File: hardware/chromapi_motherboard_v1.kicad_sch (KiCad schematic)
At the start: 8 parts

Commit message: Annotating components
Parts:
- renumbered FID3 to FID2, FID2 to FID3, TP10 to TP1
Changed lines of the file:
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@@
 		(dnp no)
 		(fields_autoplaced yes)
-		(property "Reference" "#FLG04"
+		(property "Reference" "#FLG01"
 			(at 162.56 186.055 0)
 			(effects
@@
 			(project "chromapi_motherboard_v1"
 				(path "/d1a31f26-03e0-43e1-89c1-031fe31befc5"
-					(reference "#FLG04")
+					(reference "#FLG01")
 					(unit 1)
 				)
@@
 		(dnp no)
 		(fields_autoplaced yes)
-		(property "Reference" "FID2"
+		(property "Reference" "FID3"
 			(at 128.27 175.2599 0)
 			(effects
@@
 			(project "chromapi_motherboard_v1"
 				(path "/d1a31f26-03e0-43e1-89c1-031fe31befc5"
-					(reference "FID2")
+					(reference "FID3")
 					(unit 1)
 				)
@@
 		(dnp no)
 		(fields_autoplaced yes)
-		(property "Reference" "FID3"
+		(property "Reference" "FID2"
 			(at 123.19 182.8799 0)
 			(effects
@@
 			(project "chromapi_motherboard_v1"
 				(path "/d1a31f26-03e0-43e1-89c1-031fe31befc5"
-					(reference "FID3")
+					(reference "FID2")
 					(unit 1)
 				)
@@
 		(dnp no)
 		(fields_autoplaced yes)
-		(property "Reference" "TP10"
+		(property "Reference" "TP1"
 			(at 137.668 177.8 90)
 			(effects
@@
 			(project ""
 				(path "/d1a31f26-03e0-43e1-89c1-031fe31befc5"
-					(reference "TP10")
-					(unit 1)
-				)
+					(reference "TP1")
+					(unit 1)
+				)

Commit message: Adding footprint & symbol folders
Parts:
- renumbered FID3 to FID2, FID2 to FID3
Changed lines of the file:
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@@
 		(dnp no)
 		(fields_autoplaced yes)
-		(property "Reference" "FID3"
+		(property "Reference" "FID2"
 			(at 128.27 175.2599 0)
 			(effects
@@
 			(project "chromapi_motherboard_v1"
 				(path "/d1a31f26-03e0-43e1-89c1-031fe31befc5"
-					(reference "FID3")
+					(reference "FID2")
 					(unit 1)
 				)
@@
 		(dnp no)
 		(fields_autoplaced yes)
-		(property "Reference" "FID2"
+		(property "Reference" "FID3"
 			(at 123.19 182.8799 0)
 			(effects
@@
 			(project "chromapi_motherboard_v1"
 				(path "/d1a31f26-03e0-43e1-89c1-031fe31befc5"
-					(reference "FID2")
+					(reference "FID3")
 					(unit 1)
 				)

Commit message: Updating footprints
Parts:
- FID1, FID2, FID3: footprint (none) -> Fiducial:Fiducial_1mm_Mask2mm
- H1, H2, H3, H4: footprint (none) -> MountingHole:MountingHole_2.7mm_M2.5_ISO14580_Pad_TopBottom
- TP1: footprint (none) -> TestPoint:TestPoint_Pad_D1.5mm
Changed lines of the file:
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@@
 			)
 		)
-		(property "Footprint" ""
+		(property "Footprint" "MountingHole:MountingHole_2.7mm_M2.5_ISO14580_Pad_TopBottom"
 			(at 156.21 177.8 0)
 			(effects
@@
 			)
 		)
-		(property "Footprint" ""
+		(property "Footprint" "Fiducial:Fiducial_1mm_Mask2mm"
 			(at 125.73 176.53 0)
 			(effects
@@
 			)
 		)
-		(property "Footprint" ""
+		(property "Footprint" "MountingHole:MountingHole_2.7mm_M2.5_ISO14580_Pad_TopBottom"
 			(at 149.86 177.8 0)
 			(effects
@@
 			)
 		)
-		(property "Footprint" ""
+		(property "Footprint" "Fiducial:Fiducial_1mm_Mask2mm"
 			(at 120.65 184.15 0)
 			(effects
@@
 			)
 		)
-		(property "Footprint" ""
+		(property "Footprint" "Fiducial:Fiducial_1mm_Mask2mm"
 			(at 115.57 176.53 0)
 			(effects
@@
 			)
 		)
-		(property "Footprint" ""
+		(property "Footprint" "MountingHole:MountingHole_2.7mm_M2.5_ISO14580_Pad_TopBottom"
 			(at 143.51 177.8 0)
 			(effects
@@
 			)
 		)
-		(property "Footprint" ""
+		(property "Footprint" "TestPoint:TestPoint_Pad_D1.5mm"
 			(at 140.97 177.8 0)
 			(effects
@@
 			)
 		)
-		(property "Footprint" ""
+		(property "Footprint" "MountingHole:MountingHole_2.7mm_M2.5_ISO14580_Pad_TopBottom"
 			(at 162.56 177.8 0)
 			(effects

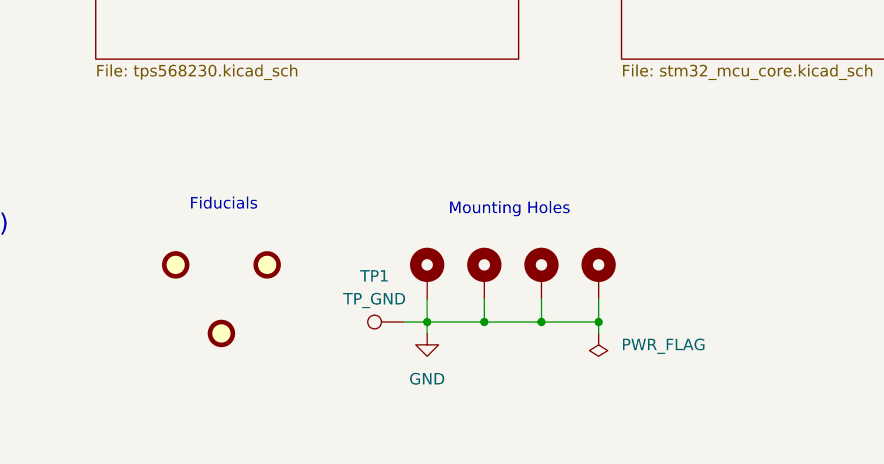
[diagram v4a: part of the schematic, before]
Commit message: adding chromapi logo to library
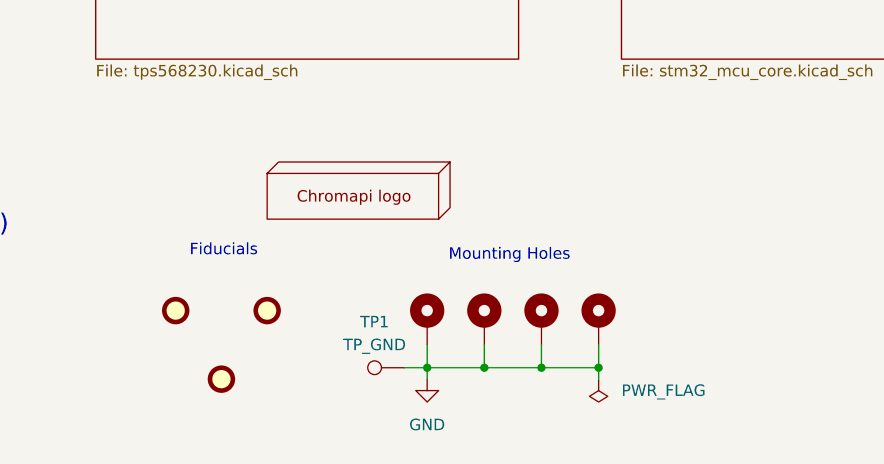
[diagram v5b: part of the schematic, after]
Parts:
- added H1: ~, Chromapi_FP:chromapi_logo, symbol chromapi_logo:Chromapi_Logo
- renumbered H1 to H2, H2 to H3, H3 to H4, H4 to H5
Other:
- moved on the sheet: TP1

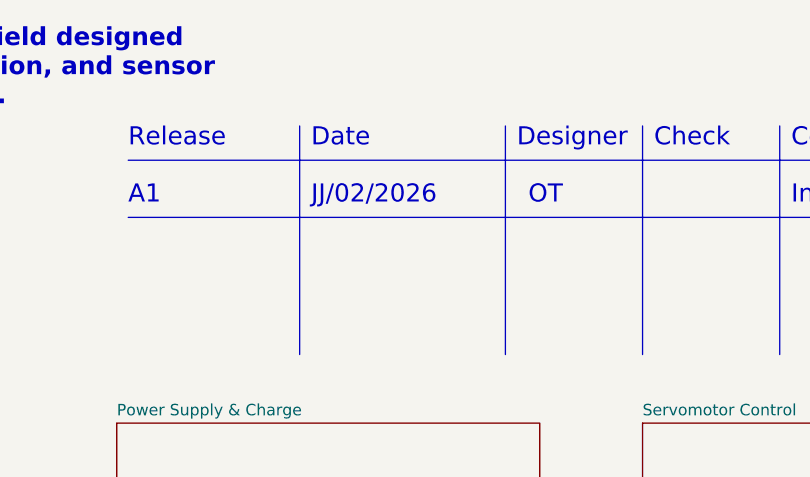
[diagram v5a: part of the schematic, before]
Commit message: Applying first corrections from first review
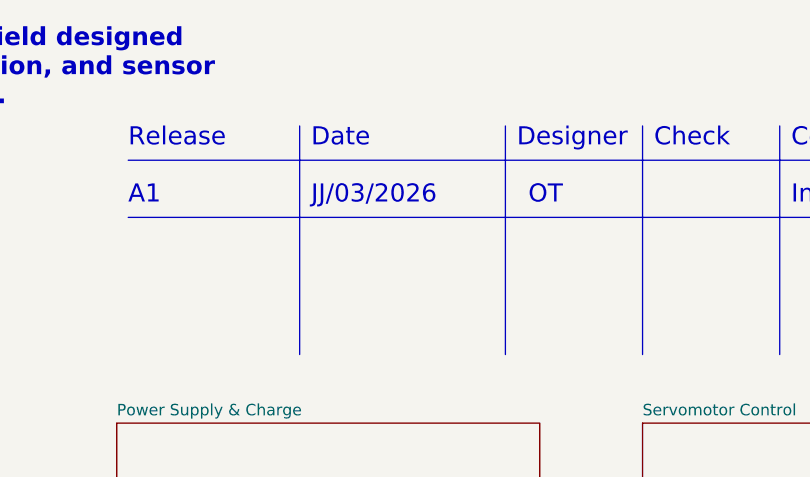
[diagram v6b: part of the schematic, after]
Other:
- note added: "JJ/03/2026"
- note removed: "JJ/02/2026"
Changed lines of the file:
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@@
 		)
 	)
-	(text "JJ/02/2026"
+	(text "JJ/03/2026"
 		(exclude_from_sim no)
 		(at 128.27 35.56 0)

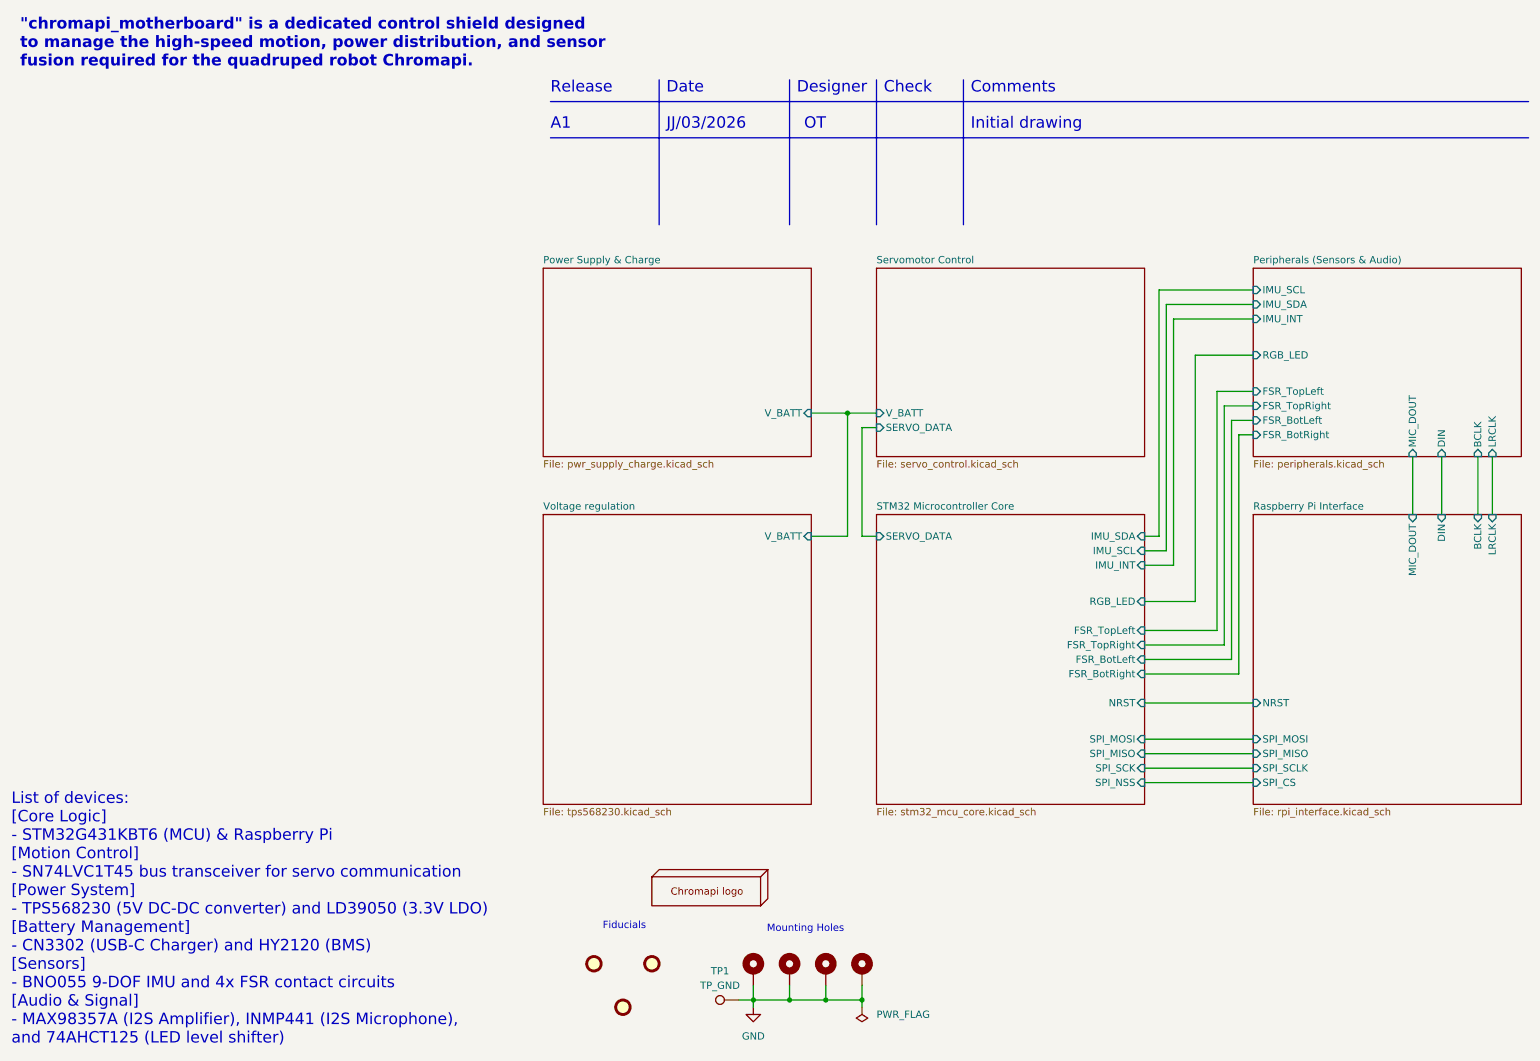
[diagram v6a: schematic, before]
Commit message: Schematic servo tranceiver correction
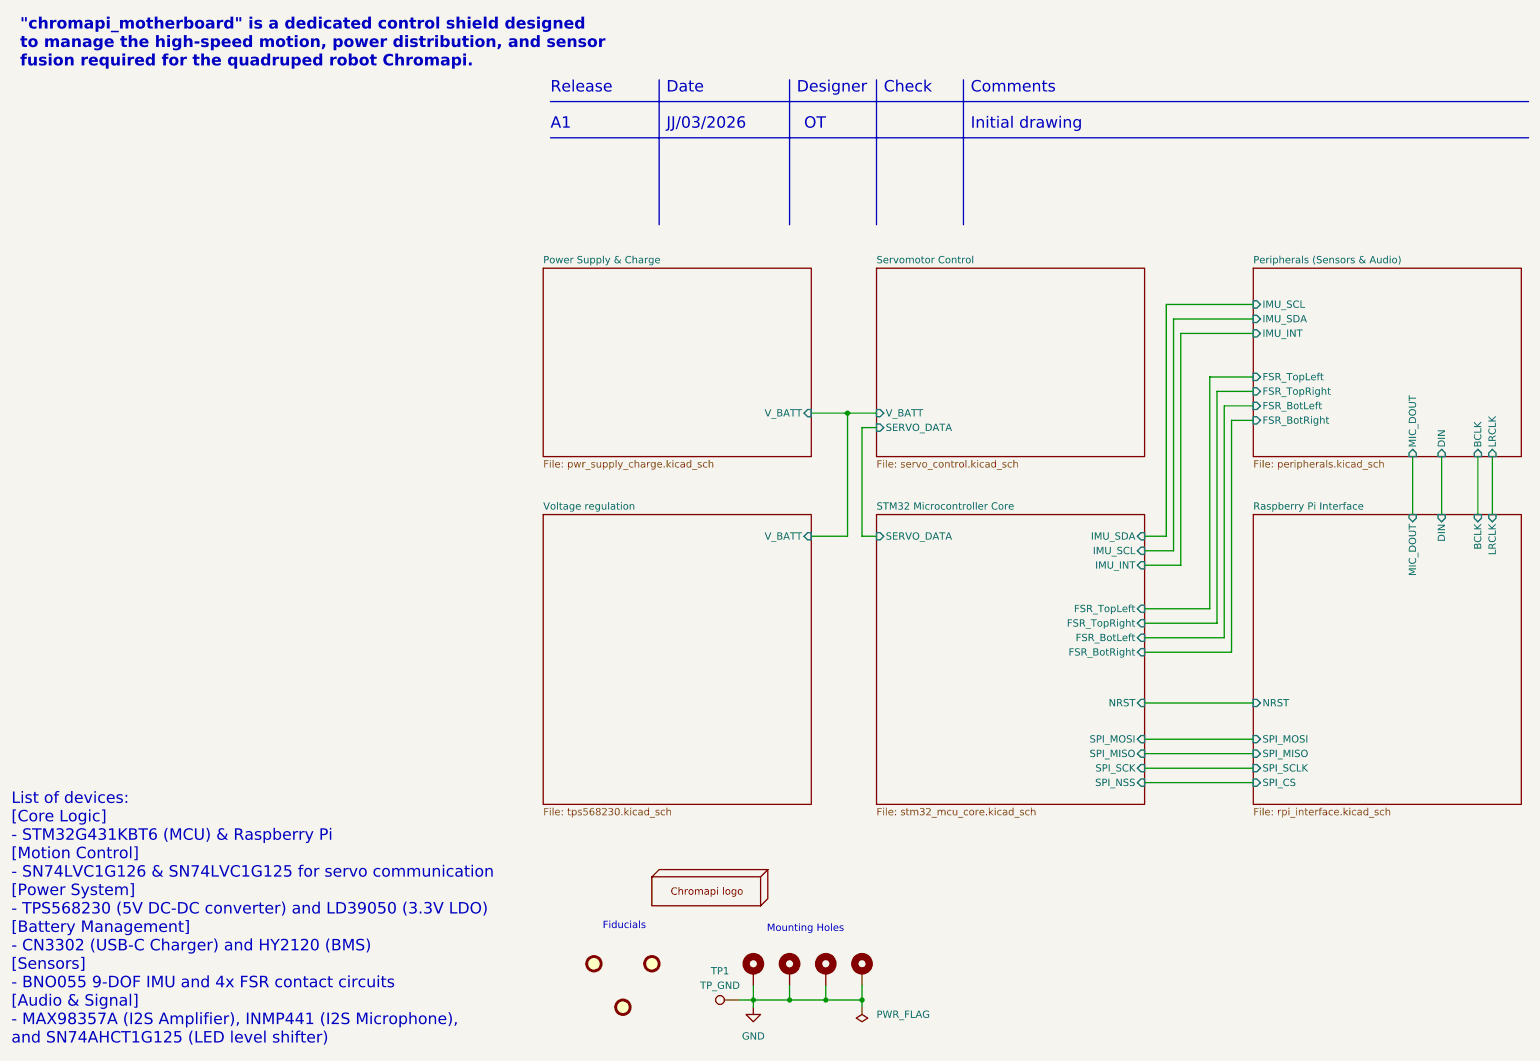
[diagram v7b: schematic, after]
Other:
- sheet Peripherals (Sensors & Audio) ports: added none; removed RGB_LED
- sheet STM32 Microcontroller Core ports: added none; removed RGB_LED
- note added: "List of devices: [Core Logic] - STM32G431KBT6 (MCU) & Raspberry Pi [Motion Control] - SN74LVC1G126 & SN74LVC1G125 for servo communication [Power System] - TPS568230 (5V DC-DC converter) and LD39050 (3.3V LDO) [Battery Management] - CN3302 (USB-C Charger) and HY2120 (BMS) [Sensors] - BNO055 9-DOF IMU and 4x FSR contact circuits [Audio & Signal] - MAX98357A (I2S Amplifier), INMP441 (I2S Microphone)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"
- note removed: "List of devices: [Core Logic] - STM32G431KBT6 (MCU) & Raspberry Pi [Motion Control] - SN74LVC1T45 bus transceiver for servo communication [Power System] - TPS568230 (5V DC-DC converter) and LD39050 (3.3V LDO) [Battery Management] - CN3302 (USB-C Charger) and HY2120 (BMS) [Sensors] - BNO055 9-DOF IMU and 4x FSR contact circuits [Audio & Signal] - MAX98357A (I2S Amplifier), INMP441 (I2S Microphone)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"
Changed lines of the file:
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@@
 		)
 	)
-	(text "List of devices:\n[Core Logic] \n- STM32G431KBT6 (MCU) & Raspberry Pi\n[Motion Control] \n- SN74LVC1T45 bus transceiver for servo communication\n[Power System] \n- TPS568230 (5V DC-DC converter) and LD39050 (3.3V LDO)\n[Battery Management] \n- CN3302 (USB-C Charger) and HY2120 (BMS)\n[Sensors] \n- BNO055 9-DOF IMU and 4x FSR contact circuits\n[Audio & Signal] \n- MAX98357A (I2S Amplifier), INMP441 (I2S Microphone),\nand 74AHCT125 (LED level shifter)"
+	(text "List of devices:\n[Core Logic] \n- STM32G431KBT6 (MCU) & Raspberry Pi\n[Motion Control] \n- SN74LVC1G126 & SN74LVC1G125 for servo communication\n[Power System] \n- TPS568230 (5V DC-DC converter) and LD39050 (3.3V LDO)\n[Battery Management] \n- CN3302 (USB-C Charger) and HY2120 (BMS)\n[Sensors] \n- BNO055 9-DOF IMU and 4x FSR contact circuits\n[Audio & Signal] \n- MAX98357A (I2S Amplifier), INMP441 (I2S Microphone),\nand SN74AHCT1G125 (LED level shifter)"
 		(exclude_from_sim no)
 		(at 13.462 173.736 0)
@@
 	(wire
 		(pts
-			(xy 212.09 106.68) (xy 214.63 106.68)
+			(xy 212.09 106.68) (xy 215.9 106.68)
 		)
 		(stroke
@@
 	(wire
 		(pts
-			(xy 227.33 86.36) (xy 227.33 128.27)
+			(xy 226.06 83.82) (xy 226.06 124.46)
 		)
 		(stroke
@@
 	(wire
 		(pts
-			(xy 215.9 109.22) (xy 215.9 66.04)
+			(xy 217.17 109.22) (xy 217.17 68.58)
 		)
 		(stroke
@@
 	(wire
 		(pts
-			(xy 217.17 111.76) (xy 212.09 111.76)
+			(xy 218.44 111.76) (xy 212.09 111.76)
 		)
 		(stroke
@@
 	(wire
 		(pts
-			(xy 231.14 83.82) (xy 226.06 83.82)
+			(xy 231.14 81.28) (xy 224.79 81.28)
 		)
 		(stroke
@@
 	(wire
 		(pts
-			(xy 227.33 128.27) (xy 212.09 128.27)
+			(xy 226.06 124.46) (xy 212.09 124.46)
 		)
 		(stroke
@@
 	(wire
 		(pts
-			(xy 212.09 118.11) (xy 220.98 118.11)
-		)
-		(stroke
-			(width 0)
-			(type default)
-		)
-	)
-	(wire
-		(pts
-			(xy 231.14 68.58) (xy 217.17 68.58)
+			(xy 231.14 71.12) (xy 218.44 71.12)
 		)
 		(stroke
@@
 	(wire
 		(pts
-			(xy 214.63 106.68) (xy 214.63 63.5)
+			(xy 215.9 106.68) (xy 215.9 66.04)
 		)
 		(stroke
@@
 	(wire
 		(pts
-			(xy 217.17 68.58) (xy 217.17 111.76)
+			(xy 218.44 71.12) (xy 218.44 111.76)
 		)
 		(stroke
@@
 	(wire
 		(pts
-			(xy 231.14 86.36) (xy 227.33 86.36)
+			(xy 231.14 83.82) (xy 226.06 83.82)
 		)
 		(stroke
@@
 	(wire
 		(pts
-			(xy 220.98 74.93) (xy 231.14 74.93)
-		)
-		(stroke
-			(width 0)
-			(type default)
-		)
-	)
-	(wire
-		(pts
 			(xy 259.08 92.71) (xy 259.08 102.87)
 		)
@@
 	(wire
 		(pts
-			(xy 228.6 130.81) (xy 228.6 88.9)
+			(xy 227.33 127) (xy 227.33 86.36)
 		)
 		(stroke
@@
 	(wire
 		(pts
-			(xy 226.06 83.82) (xy 226.06 125.73)
+			(xy 224.79 81.28) (xy 224.79 121.92)
 		)
 		(stroke
@@
 	(wire
 		(pts
-			(xy 224.79 81.28) (xy 231.14 81.28)
+			(xy 223.52 78.74) (xy 231.14 78.74)
 		)
 		(stroke
@@
 	(wire
 		(pts
-			(xy 220.98 118.11) (xy 220.98 74.93)
-		)
-		(stroke
-			(width 0)
-			(type default)
-		)
-	)
-	(wire
-		(pts
 			(xy 212.09 144.78) (xy 231.14 144.78)
 		)
@@
 	(wire
 		(pts
-			(xy 228.6 88.9) (xy 231.14 88.9)
+			(xy 227.33 86.36) (xy 231.14 86.36)
 		)
 		(stroke
@@
 	(wire
 		(pts
-			(xy 214.63 63.5) (xy 231.14 63.5)
+			(xy 215.9 66.04) (xy 231.14 66.04)
 		)
 		(stroke
@@
 	(wire
 		(pts
-			(xy 224.79 123.19) (xy 224.79 81.28)
+			(xy 223.52 119.38) (xy 223.52 78.74)
 		)
 		(stroke
@@
 	(wire
 		(pts
-			(xy 212.09 123.19) (xy 224.79 123.19)
+			(xy 212.09 119.38) (xy 223.52 119.38)
 		)
 		(stroke
@@
 	(wire
 		(pts
-			(xy 212.09 109.22) (xy 215.9 109.22)
+			(xy 212.09 109.22) (xy 217.17 109.22)
 		)
 		(stroke
@@
 	(wire
 		(pts
-			(xy 215.9 66.04) (xy 231.14 66.04)
+			(xy 217.17 68.58) (xy 231.14 68.58)
 		)
 		(stroke
@@
 	(wire
 		(pts
-			(xy 212.09 130.81) (xy 228.6 130.81)
+			(xy 212.09 127) (xy 227.33 127)
 		)
 		(stroke
@@
 	(wire
 		(pts
-			(xy 226.06 125.73) (xy 212.09 125.73)
+			(xy 224.79 121.92) (xy 212.09 121.92)
 		)
 		(stroke
@@
 		)
 		(pin "FSR_TopRight" input
-			(at 212.09 125.73 0)
+			(at 212.09 121.92 0)
 			(effects
 				(font
@@
 		)
 		(pin "FSR_TopLeft" input
-			(at 212.09 123.19 0)
+			(at 212.09 119.38 0)
 			(effects
 				(font
@@
 		)
 		(pin "FSR_BotLeft" input
-			(at 212.09 128.27 0)
-			(effects
-				(font
-					(size 1.27 1.27)
-				)
-				(justify right)
-			)
-		)
-		(pin "RGB_LED" input
-			(at 212.09 118.11 0)
+			(at 212.09 124.46 0)
 			(effects
 				(font
@@
 		)
 		(pin "FSR_BotRight" input
-			(at 212.09 130.81 0)
+			(at 212.09 127 0)
 			(effects
 				(font
@@
 			)
 		)
-		(pin "RGB_LED" input
-			(at 231.14 74.93 180)
-			(effects
-				(font
-					(size 1.27 1.27)
-				)
-				(justify left)
-			)
-		)
 		(pin "FSR_TopLeft" input
-			(at 231.14 81.28 180)
+			(at 231.14 78.74 180)
 			(effects
 				(font
@@
 		)
 		(pin "FSR_TopRight" input
-			(at 231.14 83.82 180)
+			(at 231.14 81.28 180)
 			(effects
 				(font
@@
 		)
 		(pin "IMU_SCL" input
-			(at 231.14 63.5 180)
+			(at 231.14 66.04 180)
 			(effects
 				(font
@@
 		)
 		(pin "IMU_INT" input
-			(at 231.14 68.58 180)
+			(at 231.14 71.12 180)
 			(effects
 				(font
@@
 		)
 		(pin "FSR_BotLeft" input
-			(at 231.14 86.36 180)
+			(at 231.14 83.82 180)
 			(effects
 				(font
@@
 		)
 		(pin "FSR_BotRight" input
-			(at 231.14 88.9 180)
+			(at 231.14 86.36 180)
 			(effects
 				(font
@@
 		)
 		(pin "IMU_SDA" input
-			(at 231.14 66.04 180)
+			(at 231.14 68.58 180)
 			(effects
 				(font
